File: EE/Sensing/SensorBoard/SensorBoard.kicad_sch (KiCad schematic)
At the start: 23 parts, among them J1 Conn_01x04_Male, Q11 DMP31D1U-7, Q12 DMP31D1U-7, U1 TCR2EE27, U2 TCR2EE32, U3 TCA9555PWR

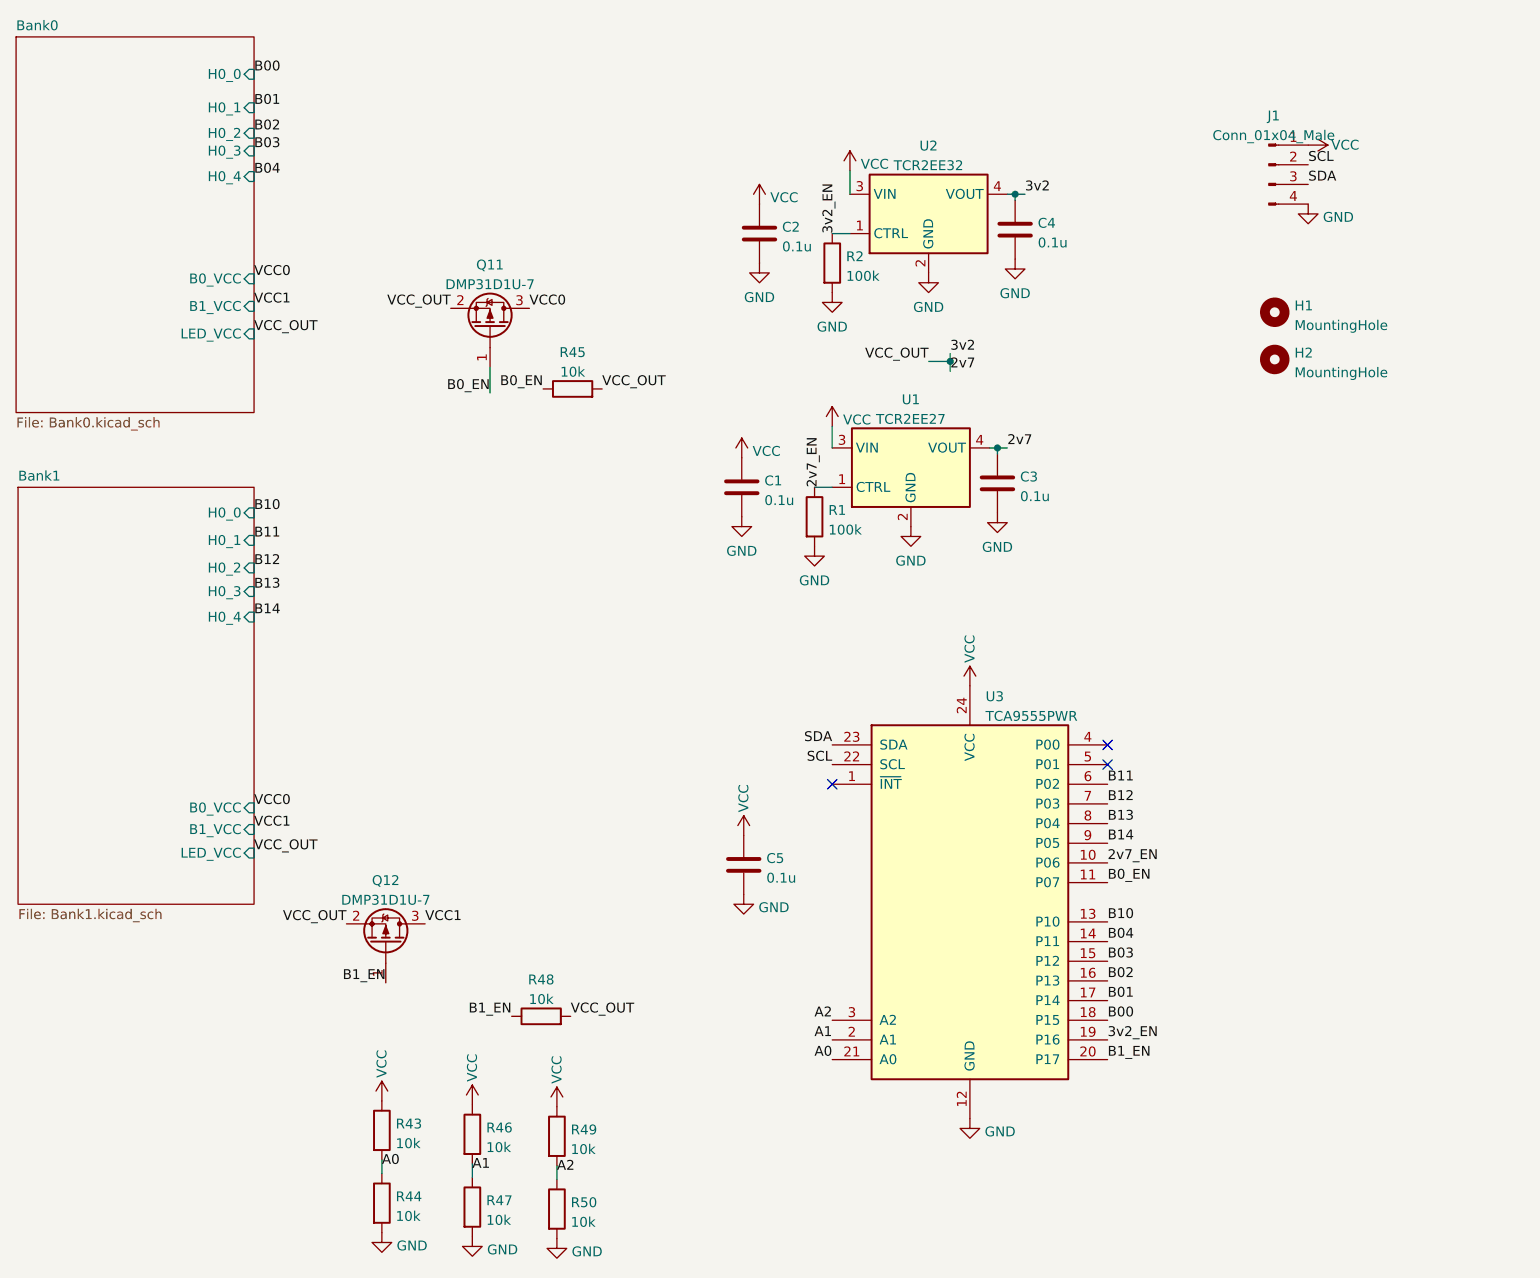
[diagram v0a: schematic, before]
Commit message: Replacement after sensing change
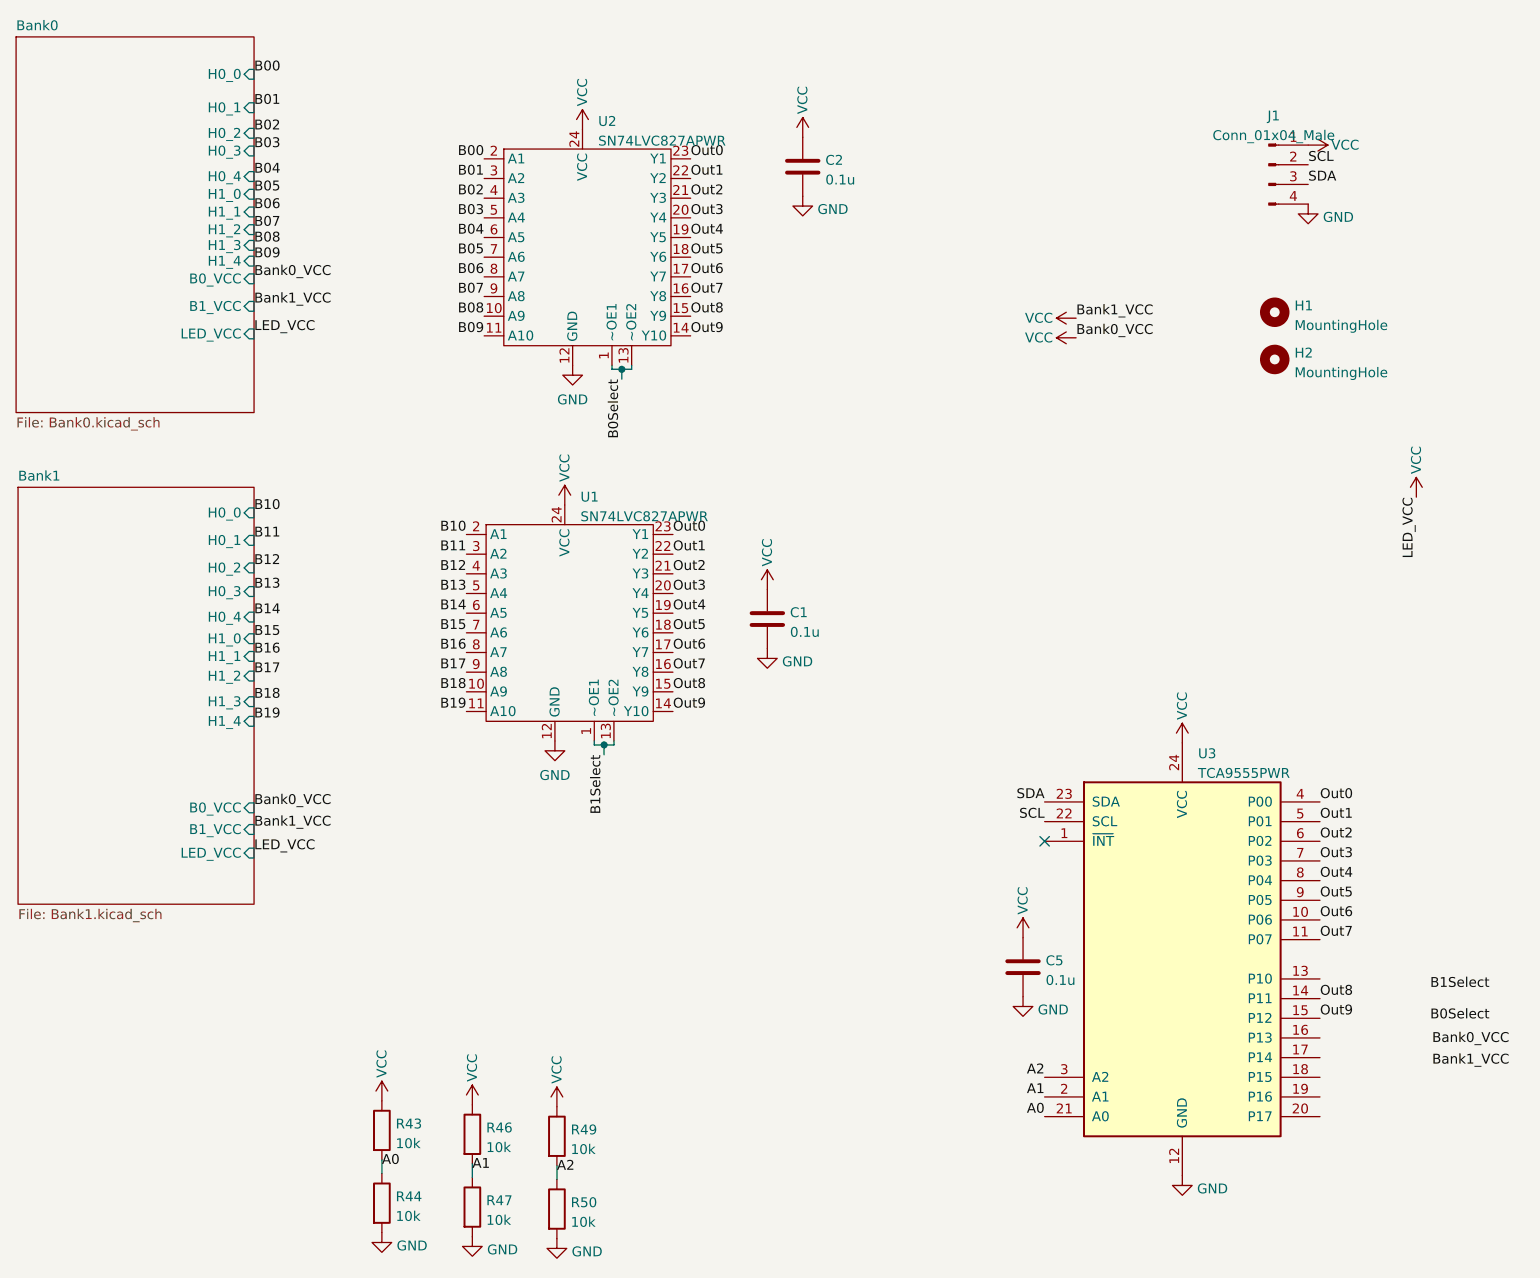
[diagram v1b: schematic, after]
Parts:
- removed C3, C4: 0.1u, Capacitor_SMD:C_0402_1005Metric_Pad0.74x0.62mm_HandSolder, symbol Device:C
- removed Q11, Q12: DMP31D1U-7, Package_TO_SOT_SMD:SC-59, symbol Device:Q_PMOS_GSD
- removed R1, R2: 100k, Resistor_SMD:R_0402_1005Metric_Pad0.72x0.64mm_HandSolder, symbol Device:R
- removed R45, R48: 10k, Resistor_SMD:R_0402_1005Metric, symbol Device:R
- removed U1: TCR2EE27, Package_TO_SOT_SMD:SOT-553, symbol Regulator_Linear:TCR2EE27
- removed U2: TCR2EE32, Package_TO_SOT_SMD:SOT-553, symbol Regulator_Linear:TCR2EE27
- added U1, U2: SN74LVC827APWR, Package_SO:TSSOP-24_4.4x6.5mm_P0.5mm, symbol New_Library:SN74LVC827ADWR
- C1, C2: footprint Capacitor_SMD:C_0402_1005Metric_Pad0.74x0.62mm_HandSolder -> Capacitor_SMD:C_0402_1005Metric
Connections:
- net B00: now also U2.2 (A1); no longer U3.18 (P15)
- net B01: now also U2.3 (A2); no longer U3.17 (P14)
- net B02: now also U2.4 (A3); no longer U3.16 (P13)
- net B03: now also U2.5 (A4); no longer U3.15 (P12)
- net B04: now also U2.6 (A5); no longer U3.14 (P11)
- net B10: now also U1.2 (A1); no longer U3.13 (P10)
- net B11: now also U1.3 (A2); no longer U3.6 (P02)
- net B12: now also U1.4 (A3); no longer U3.7 (P03)
- net B13: now also U1.5 (A4); no longer U3.8 (P04)
- net B14: now also U1.6 (A5); no longer U3.9 (P05)
- net GND: now also U1.12 (GND), U2.12 (GND)
- net VCC: now also U1.24 (VCC), U2.24 (VCC)
- net Out0: now reaches U3.4 (P00)
- net Out0: now also U1.23 (Y1), U2.23 (Y1)
- net Out1: now reaches U3.5 (P01)
- net Out1: now also U1.22 (Y2), U2.22 (Y2)
- net 2v7_EN renamed Out6
- net Out6: now also U1.17 (Y7), U2.17 (Y7)
- net 3v2_EN: no longer names the net of U3.19 (P16)
- net B0_EN renamed Out7
- net Out7: now also U1.16 (Y8), U2.16 (Y8)
- net B1_EN: no longer names the net of U3.20 (P17)
- new net B05: U2.7 (A6)
- new net B06: U2.8 (A7)
- new net B07: U2.9 (A8)
- new net B08: U2.10 (A9)
- new net B09: U2.11 (A10)
- new net B0Select: U2.1 (~OE1), U2.13 (~OE2)
- new net B15: U1.7 (A6)
- new net B16: U1.8 (A7)
- new net B17: U1.9 (A8)
- new net B18: U1.10 (A9)
- new net B19: U1.11 (A10)
- new net B1Select: U1.1 (~OE1), U1.13 (~OE2)
- new net Out2: U1.21 (Y3), U2.21 (Y3), U3.6 (P02)
- new net Out3: U1.20 (Y4), U2.20 (Y4), U3.7 (P03)
- new net Out4: U1.19 (Y5), U2.19 (Y5), U3.8 (P04)
- new net Out5: U1.18 (Y6), U2.18 (Y6), U3.9 (P05)
- new net Out8: U1.15 (Y9), U2.15 (Y9), U3.14 (P11)
- new net Out9: U1.14 (Y10), U2.14 (Y10), U3.15 (P12)
- no-connect marks 3 -> 1
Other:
- sheet Bank0 ports: added H1_0, H1_1, H1_2, H1_3, H1_4; removed none
- sheet Bank1 ports: added H1_0, H1_1, H1_2, H1_3, H1_4; removed none
- moved on the sheet: C5, U3

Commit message: Potential Layout - Inverted 1 chip for layout
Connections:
- net B01: now also U2.4 (A3); no longer U2.3 (A2)
- net B02: now also U2.6 (A5); no longer U2.4 (A3)
- net B03: now also U2.8 (A7); no longer U2.5 (A4)
- net B04: now also U2.11 (A10); no longer U2.6 (A5)
- net B05: now also U2.3 (A2); no longer U2.7 (A6)
- net B06: now also U2.5 (A4); no longer U2.8 (A7)
- net B07: now also U2.7 (A6); no longer U2.9 (A8)
- net B08: now also U2.9 (A8); no longer U2.10 (A9)
- net B09: now also U2.10 (A9); no longer U2.11 (A10)
- net B0Select: now also U3.19 (P16)
- net B10: now also U1.3 (A2); no longer U1.2 (A1)
- net B11: now also U1.4 (A3); no longer U1.3 (A2)
- net B12: now also U1.6 (A5); no longer U1.4 (A3)
- net B13: now also U1.8 (A7); no longer U1.5 (A4)
- net B14: now also U1.10 (A9); no longer U1.6 (A5)
- net B15: now also U1.2 (A1); no longer U1.7 (A6)
- net B16: now also U1.5 (A4); no longer U1.8 (A7)
- net B17: now also U1.7 (A6); no longer U1.9 (A8)
- net B18: now also U1.9 (A8); no longer U1.10 (A9)
- net B1Select: now also U3.15 (P12)
- net Out0: now also U2.14 (Y10); no longer U2.23 (Y1)
- net Out1: now also U2.15 (Y9); no longer U2.22 (Y2)
- net Out2: now also U2.16 (Y8); no longer U2.21 (Y3)
- net Out3: now also U2.17 (Y7); no longer U2.20 (Y4)
- net Out4: now also U2.18 (Y6); no longer U2.19 (Y5)
- net Out5: now also U2.19 (Y5); no longer U2.18 (Y6)
- net Out6: now also U2.20 (Y4); no longer U2.17 (Y7)
- net Out7: now also U2.21 (Y3); no longer U2.16 (Y8)
- net Out8: now also U2.22 (Y2); no longer U2.15 (Y9)
- net Out9: now also U2.23 (Y1), U3.13 (P10); no longer U2.14 (Y10), U3.15 (P12)

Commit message: Routine Update
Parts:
- U1, U2: footprint Package_SO:TSSOP-24_4.4x6.5mm_P0.5mm -> Package_SO:TSSOP-24_4.4x7.8mm_P0.65mm
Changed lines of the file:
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@@
       (effects (font (size 1.27 1.27)) (justify left))
     )
-    (property "Footprint" "Package_SO:TSSOP-24_4.4x6.5mm_P0.5mm" (id 2) (at 178.308 56.896 0)
+    (property "Footprint" "Package_SO:TSSOP-24_4.4x7.8mm_P0.65mm" (id 2) (at 178.308 56.896 0)
       (effects (font (size 1.27 1.27)) hide)
     )
@@
       (effects (font (size 1.27 1.27)) (justify left))
     )
-    (property "Footprint" "Package_SO:TSSOP-24_4.4x6.5mm_P0.5mm" (id 2) (at 180.594 8.382 0)
+    (property "Footprint" "Package_SO:TSSOP-24_4.4x7.8mm_P0.65mm" (id 2) (at 180.594 8.382 0)
       (effects (font (size 1.27 1.27)) hide)
     )
@@
     )
     (path "/044c1699-8e9d-45c5-a423-8e1c4f37231d"
-      (reference "U1") (unit 1) (value "SN74LVC827APWR") (footprint "Package_SO:TSSOP-24_4.4x6.5mm_P0.5mm")
+      (reference "U1") (unit 1) (value "SN74LVC827APWR") (footprint "Package_SO:TSSOP-24_4.4x7.8mm_P0.65mm")
     )
     (path "/a98e967b-5579-4f2c-a046-1fd406329b6c"
-      (reference "U2") (unit 1) (value "SN74LVC827APWR") (footprint "Package_SO:TSSOP-24_4.4x6.5mm_P0.5mm")
+      (reference "U2") (unit 1) (value "SN74LVC827APWR") (footprint "Package_SO:TSSOP-24_4.4x7.8mm_P0.65mm")
     )
     (path "/78d7b32d-68de-413c-bd60-8d542d1f923b"
